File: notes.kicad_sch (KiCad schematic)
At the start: 14 parts, among them J401 Conn_01x11

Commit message: :package: finished version 1.0.0, generated production files
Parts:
- gave numbers to parts that had none: 1
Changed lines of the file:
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@@
 		(on_board yes)
 		(dnp no)
-		(property "Reference" "TP?"
+		(property "Reference" "TP401"
 			(at 121.92 55.1179 0)
 			(effects
@@
 			(project ""
 				(path "/7eacce39-bbdf-4759-aeb5-d69ccfcb7b29/9b70b2fc-49e3-42a0-b447-77c1c57b7a09"
-					(reference "TP?")
+					(reference "TP401")
 					(unit 1)
 				)

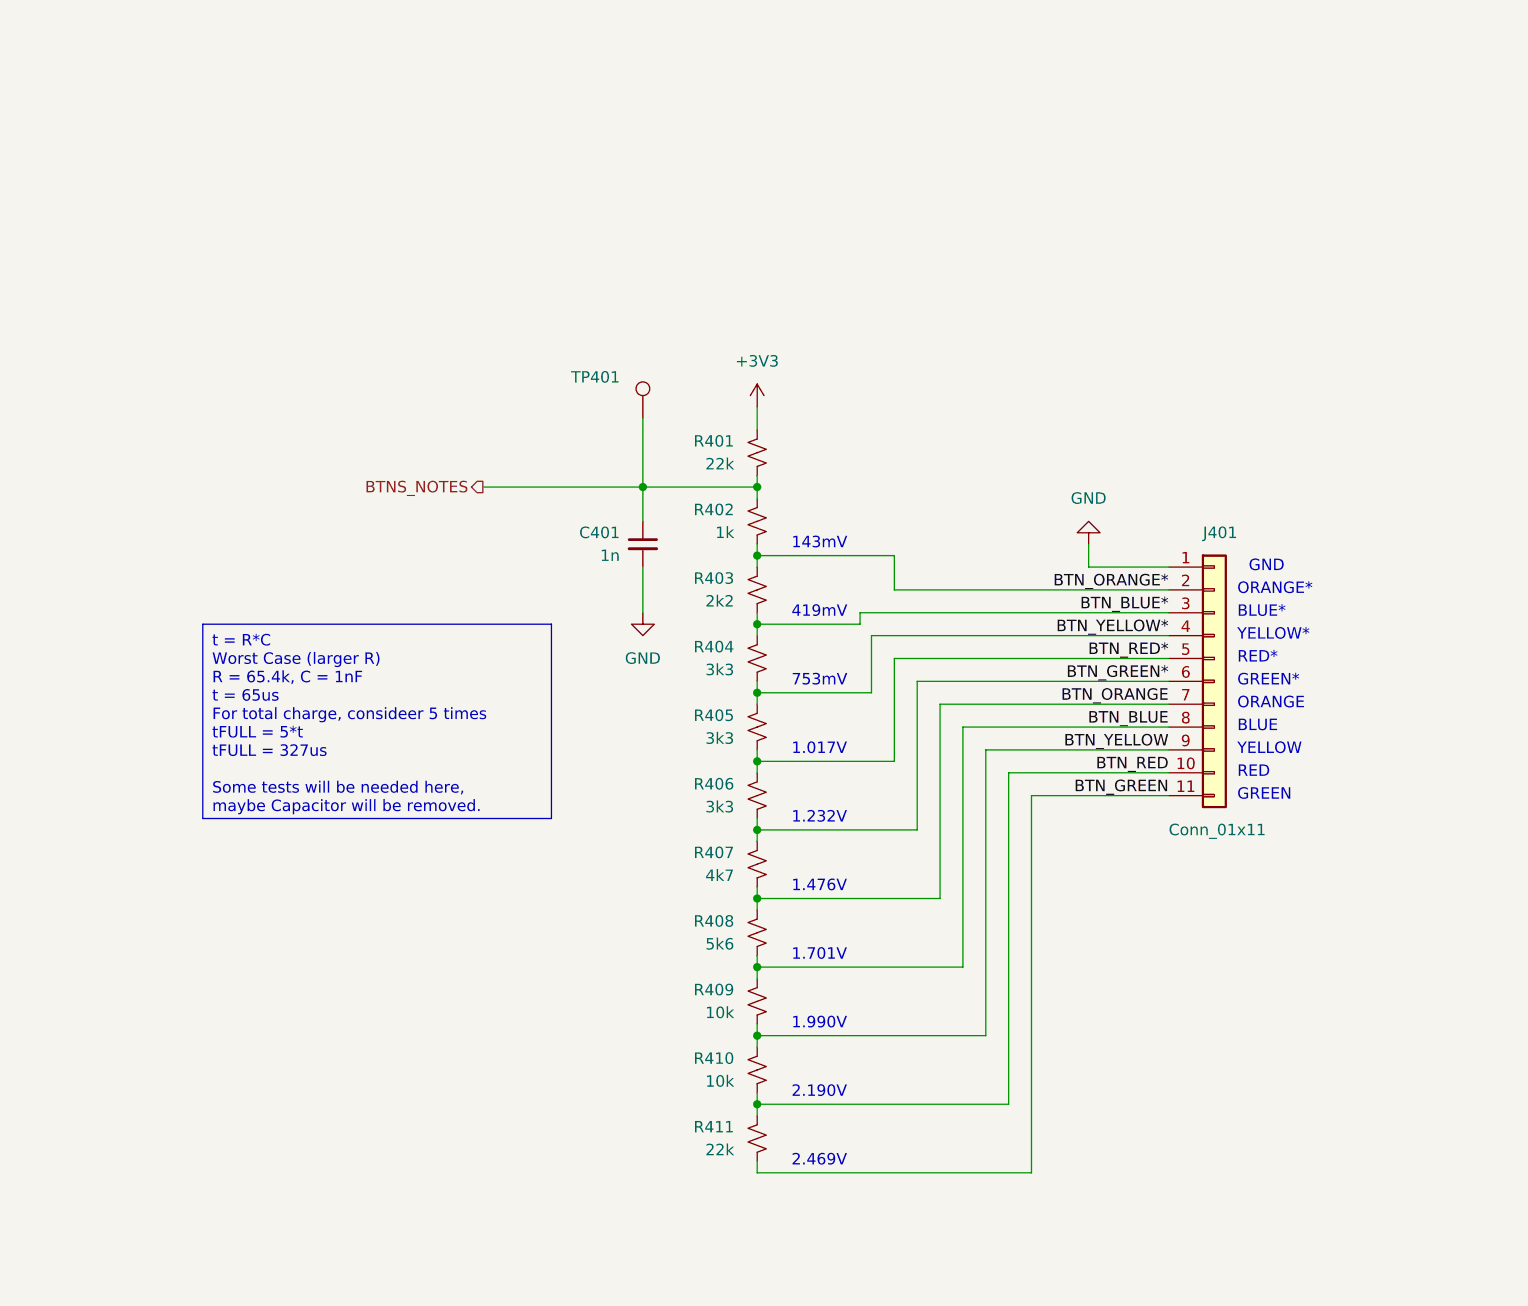
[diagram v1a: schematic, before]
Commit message: t:art: fixed noted reading, using 75hc165 for Input expander
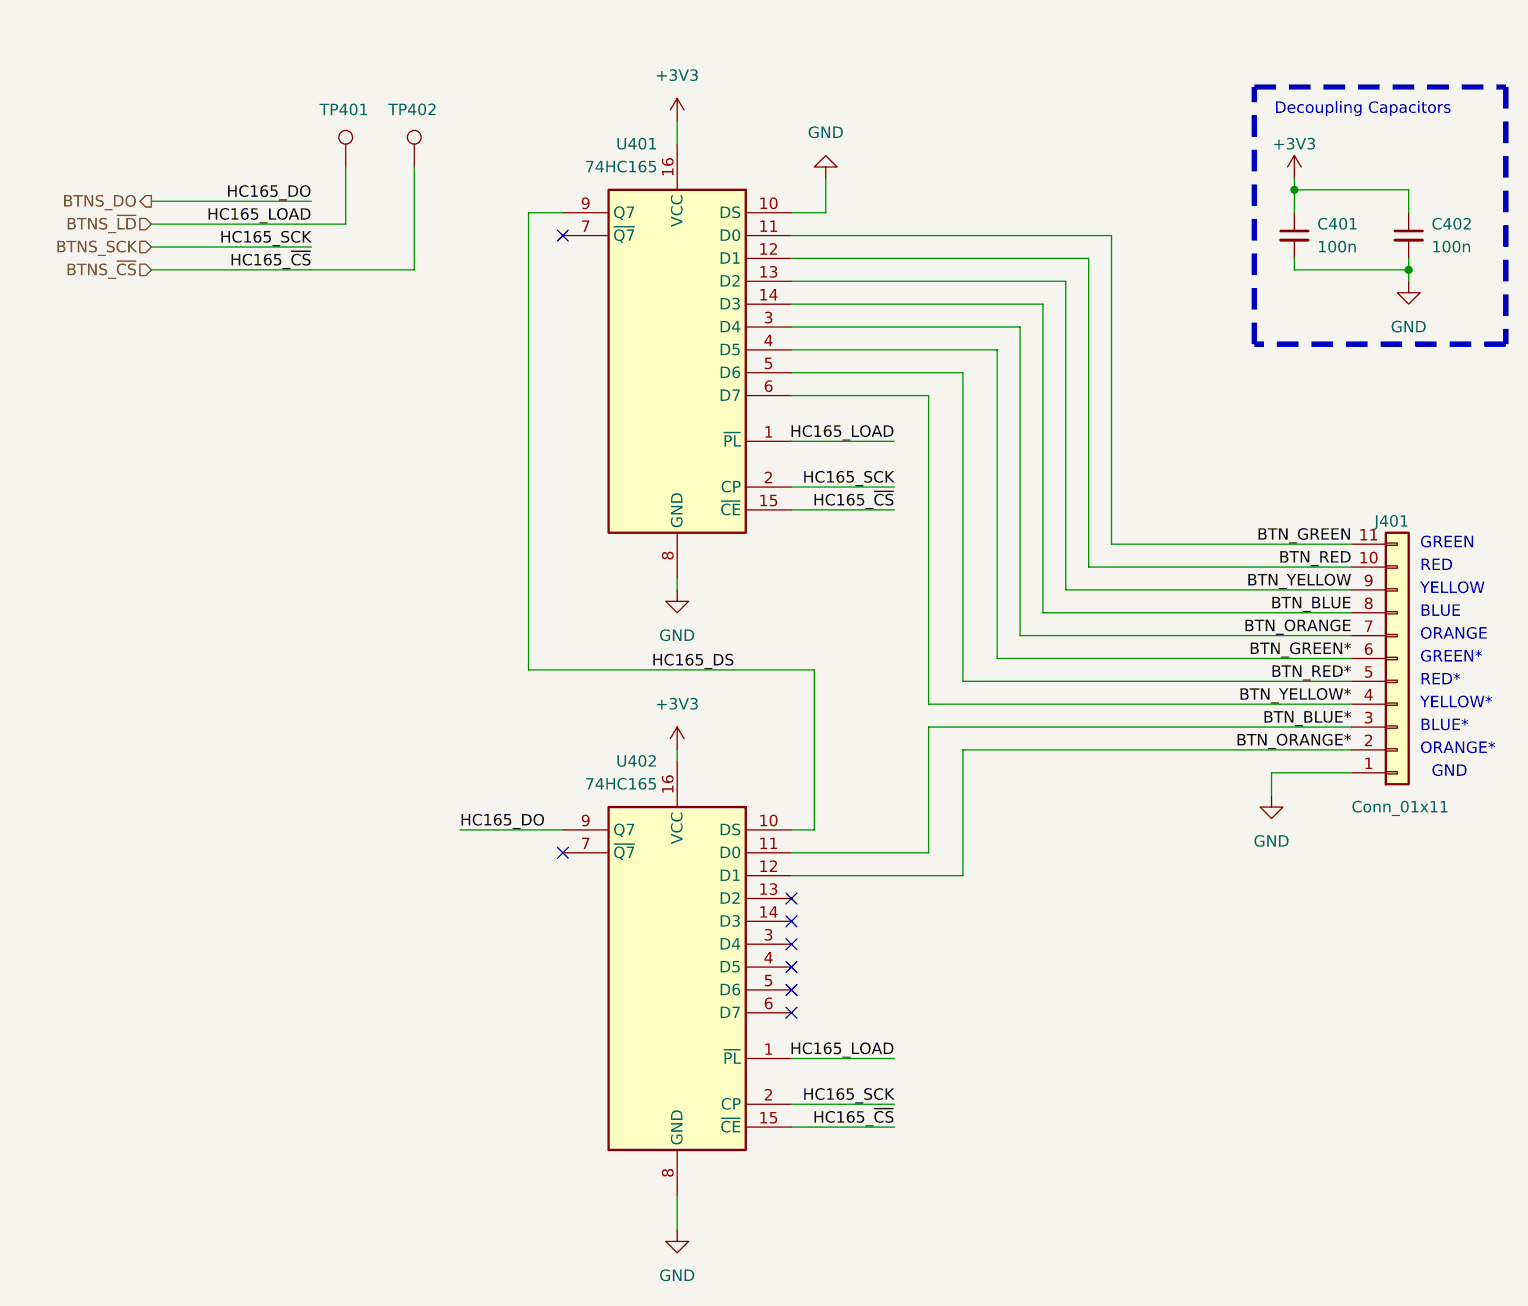
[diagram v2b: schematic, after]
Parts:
- removed R401, R411: 22k, Resistor_SMD:R_0603_1608Metric, symbol Device:R_Small_US
- removed R402: 1k, Resistor_SMD:R_0603_1608Metric, symbol Device:R_Small_US
- removed R403: 2k2, Resistor_SMD:R_0603_1608Metric, symbol Device:R_Small_US
- removed R404, R405, R406: 3k3, Resistor_SMD:R_0603_1608Metric, symbol Device:R_Small_US
- removed R407: 4k7, Resistor_SMD:R_0603_1608Metric, symbol Device:R_Small_US
- removed R408: 5k6, Resistor_SMD:R_0603_1608Metric, symbol Device:R_Small_US
- removed R409, R410: 10k, Resistor_SMD:R_0603_1608Metric, symbol Device:R_Small_US
- added C402: 100n, Capacitor_SMD:C_0603_1608Metric, symbol Device:C_Small
- added TP402: TestPoint, TestPoint:TestPoint_Pad_D1.5mm, symbol Connector:TestPoint
- added U401, U402: 74HC165, Package_SO:TSSOP-16_4.4x5mm_P0.65mm, symbol 74xx:74HC165
- C401: value 1n -> 100n; LCSC C100040 -> C14663; PN CC0603KRX7R9BB102 -> CC0603KRX7R9BB104
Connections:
- net +3V3: now also C401.1, C402.1, U401.16 (VCC), U402.16 (VCC)
- net BTN_BLUE: now also U401.14 (D3)
- net BTN_BLUE*: now also U402.11 (D0)
- net BTN_GREEN: now also U401.11 (D0)
- net BTN_GREEN*: now also U401.4 (D5)
- net BTN_ORANGE: now also U401.3 (D4)
- net BTN_ORANGE*: now also U402.12 (D1)
- net BTN_RED: now also U401.12 (D1)
- net BTN_RED*: now also U401.5 (D6)
- net BTN_YELLOW: now also U401.13 (D2)
- net BTN_YELLOW*: now also U401.6 (D7)
- net GND: now also C402.2, U401.10 (DS), U401.8 (GND), U402.8 (GND)
- net BTNS_NOTES renamed BTNS_~{LD}
- net BTNS_~{LD}: now also U401.1 (~{PL}), U402.1 (~{PL}); no longer C401.1
- new net BTNS_DO: U402.9 (Q7)
- new net BTNS_SCK: U401.2 (CP), U402.2 (CP)
- new net BTNS_~{CS}: TP402.1, U401.15 (~{CE}), U402.15 (~{CE})
- new net HC165_DS: U401.9 (Q7), U402.10 (DS)
- no-connect marks 0 -> 8
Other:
- note added: "Decoupling Capacitors"
- note removed: "1.017V"
- note removed: "1.232V"
- note removed: "1.476V"
- note removed: "1.701V"
- note removed: "1.990V"
- note removed: "143mV"
- note removed: "2.190V"
- note removed: "2.469V"
- note removed: "419mV"
- note removed: "753mV"
- moved on the sheet: J401, TP401

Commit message: small fixes
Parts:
- added R803: 4k7, Resistor_SMD:R_0603_1608Metric, symbol Device:R_Small_US
- J401: footprint Connector_JST:JST_XA_S11B-XASK-1_1x11_P2.50mm_Horizontal -> Connector_JST:JST_XH_S11B-XH-A-1_1x11_P2.50mm_Horizontal
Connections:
- net BTNS_DO: now also R803.1; no longer U402.9 (Q7)
- net GND: no longer U401.10 (DS)
- new net: R803.2, U402.9 (Q7)
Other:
- moved on the sheet: C401
